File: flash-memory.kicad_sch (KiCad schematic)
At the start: 4 parts, among them U6 W25Q64JVZEIQ

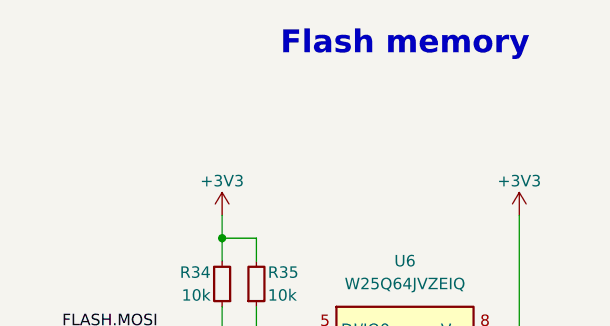
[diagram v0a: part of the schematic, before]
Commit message: [#86617] Unify captions, add TVS to USB VBUS
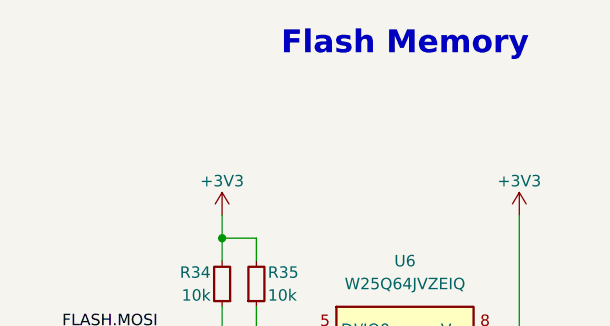
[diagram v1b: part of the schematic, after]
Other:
- note added: "Flash Memory"
- note removed: "Flash memory"
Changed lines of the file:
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@@
 		(comment 1 "www.antmicro.com")
 	)
-	(text "Flash memory"
+	(text "Flash Memory"
 		(exclude_from_sim no)
 		(at 213.36 111.76 0)

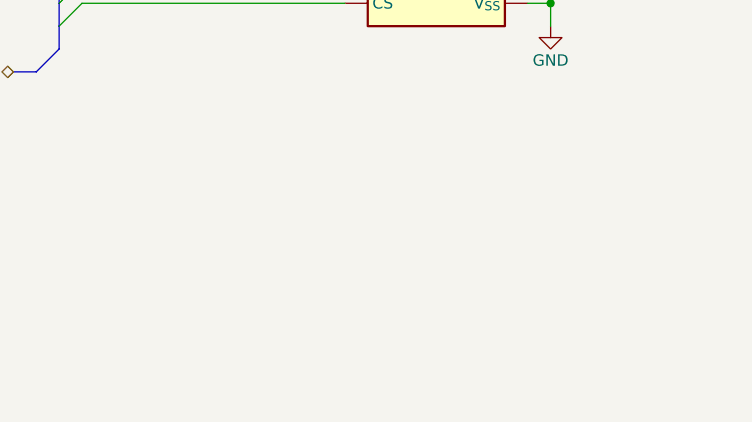
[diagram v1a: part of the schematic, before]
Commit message: [#86617] Add Tag-Connect to flash memory
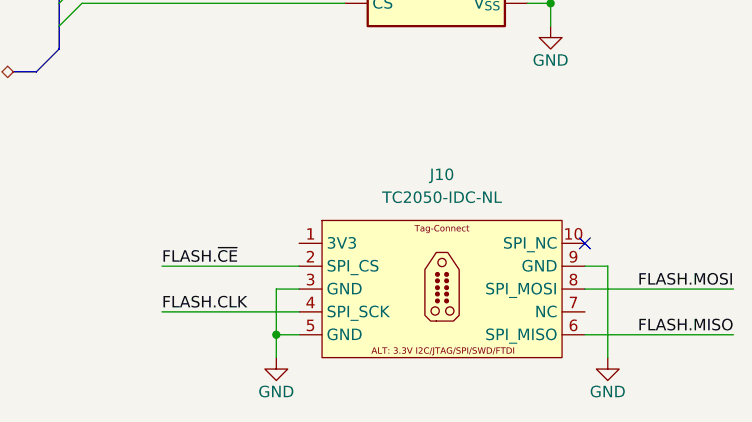
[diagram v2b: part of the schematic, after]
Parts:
- added J10: Tag-Connect_TC2050-IDC-NL_2x5_P1.27mm, antmicro-footprints:Tag-Connect_TC2050-IDC-NL_2x5_P1.27mm, symbol antmicroTestPoints:Tag-Connect_TC2050-IDC-NL_2x5_P1.27mm
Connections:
- net FLASH.CLK: now also J10.4
- net FLASH.MISO: now also J10.6
- net FLASH.MOSI: now also J10.8
- net FLASH.~{CE}: now also J10.2
- net GND: now also J10.3, J10.5, J10.9
- no-connect marks 0 -> 1

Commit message: [#86351] Rename project
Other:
- title: 10GbE Expansion -> OCuLink to 10GbE adapter
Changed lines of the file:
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@@
 	(paper "A3")
 	(title_block
-		(title "10GbE Expansion")
+		(title "OCuLink to 10GbE adapter")
 		(date "2025-11-07")
 		(rev "1.0.0")
@@
 		)
 		(instances
-			(project "10-gbe-expansion"
+			(project "OCuLink to 10GbE adapter"
 				(path "/04bda987-e5eb-48b4-9e90-d8211dc11b39/cf61e8ef-a7e0-463f-9b69-1bf3871ad792"
 					(reference "#PWR063")
@@
 		)
 		(instances
-			(project "10-gbe-expansion"
+			(project "OCuLink to 10GbE adapter"
 				(path "/04bda987-e5eb-48b4-9e90-d8211dc11b39/cf61e8ef-a7e0-463f-9b69-1bf3871ad792"
 					(reference "#PWR0338")
@@
 		)
 		(instances
-			(project "10-gbe-expansion"
+			(project "OCuLink to 10GbE adapter"
 				(path "/04bda987-e5eb-48b4-9e90-d8211dc11b39/cf61e8ef-a7e0-463f-9b69-1bf3871ad792"
 					(reference "R34")
@@
 		)
 		(instances
-			(project "10-gbe-expansion"
+			(project "OCuLink to 10GbE adapter"
 				(path "/04bda987-e5eb-48b4-9e90-d8211dc11b39/cf61e8ef-a7e0-463f-9b69-1bf3871ad792"
 					(reference "#PWR0339")
@@
 		)
 		(instances
-			(project "10-gbe-expansion"
+			(project "OCuLink to 10GbE adapter"
 				(path "/04bda987-e5eb-48b4-9e90-d8211dc11b39/cf61e8ef-a7e0-463f-9b69-1bf3871ad792"
 					(reference "#PWR064")
@@
 		)
 		(instances
-			(project "10-gbe-expansion"
+			(project "OCuLink to 10GbE adapter"
 				(path "/04bda987-e5eb-48b4-9e90-d8211dc11b39/cf61e8ef-a7e0-463f-9b69-1bf3871ad792"
 					(reference "C47")
@@
 		)
 		(instances
-			(project "10-gbe-expansion"
+			(project "OCuLink to 10GbE adapter"
 				(path "/04bda987-e5eb-48b4-9e90-d8211dc11b39/cf61e8ef-a7e0-463f-9b69-1bf3871ad792"
 					(reference "J10")
@@
 		)
 		(instances
-			(project "10-gbe-expansion"
+			(project "OCuLink to 10GbE adapter"
 				(path "/04bda987-e5eb-48b4-9e90-d8211dc11b39/cf61e8ef-a7e0-463f-9b69-1bf3871ad792"
 					(reference "#PWR065")

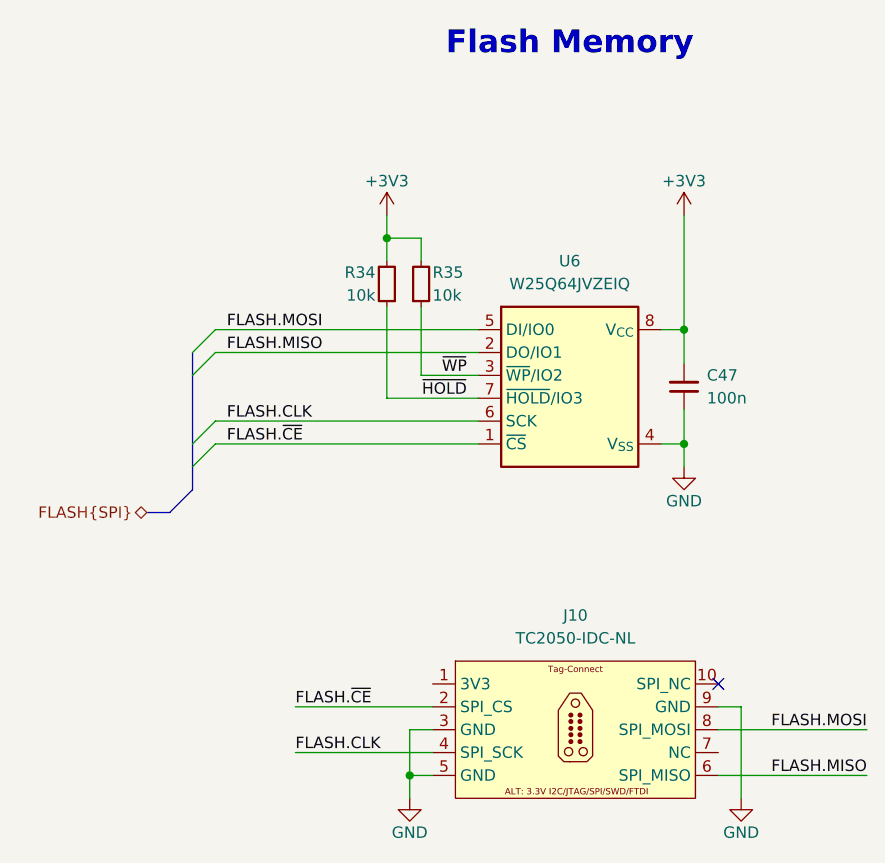
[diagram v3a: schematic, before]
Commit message: [#86617] Change flash memory to AT25DF641A-SH
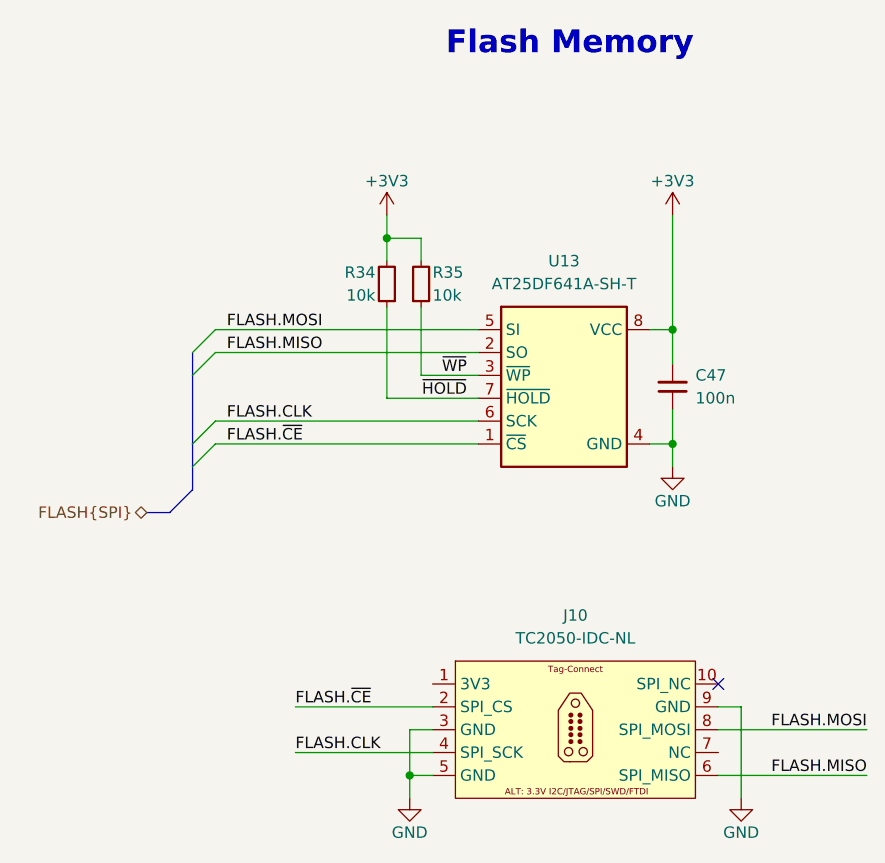
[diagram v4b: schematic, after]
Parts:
- removed U6: W25Q64JVZEIQ, antmicro-footprints:WSON-8_6x8x0.5mm_P1.27mm, symbol antmicroMemory:W25Q64JVZEIQ
- added U13: AT25DF641A-SH, antmicro-footprints:SOIC-8_5.3x5.3x2mm_P1.27mm, symbol antmicroMemory:AT25DF641A-SH
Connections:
- net +3V3: now also U13.8 (VCC)
- net FLASH.CLK: now also U13.6 (SCK)
- net FLASH.MISO: now also U13.2 (SO)
- net FLASH.MOSI: now also U13.5 (SI)
- net FLASH.~{CE}: now also U13.1 (~{CS})
- net GND: now also U13.4 (GND)
- net ~{HOLD}: now also U13.7 (~{HOLD})
- net ~{WP}: now also U13.3 (~{WP})
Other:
- moved on the sheet: C47

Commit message: [#86351] Connect Tag Connect 3V3 pin, clear ERC
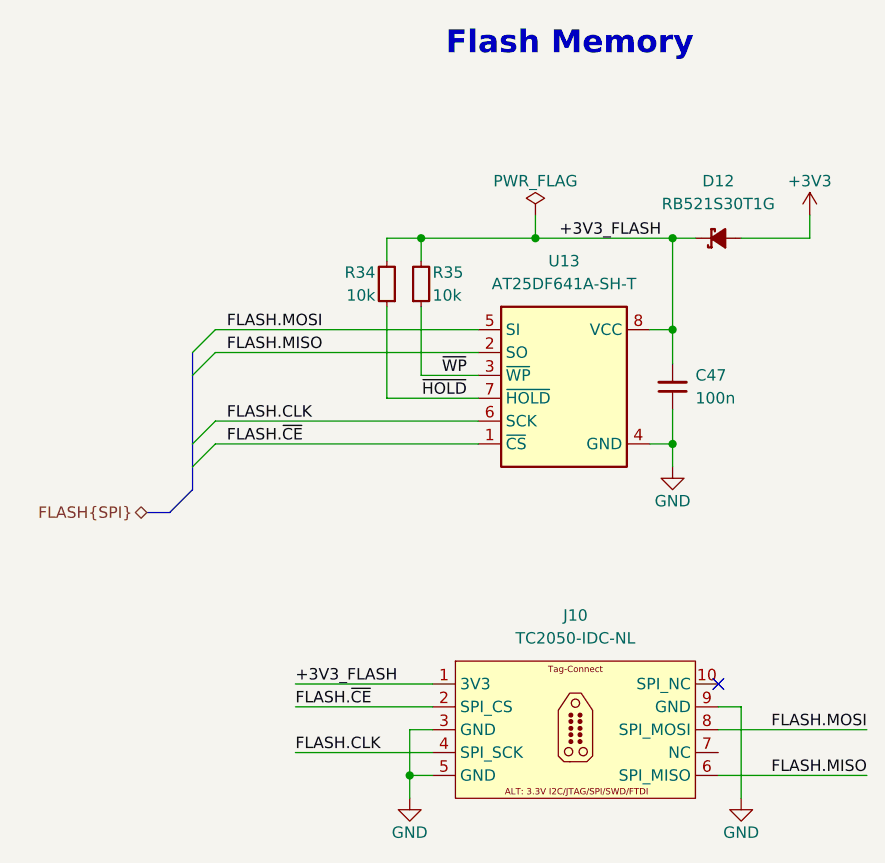
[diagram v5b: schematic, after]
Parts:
- added D12: RB521S30T1G, antmicro-footprints:SOD-523, symbol antmicroDiodesRectifiersSingle:RB521S30T1G
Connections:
- net +3V3: now also D12.2 (A); no longer C47.2, R34.2, R35.2, U13.8 (VCC)
- net +3V3_FLASH: now reaches J10.1
- net +3V3_FLASH: now also C47.2, R34.2, R35.2, U13.8 (VCC), D12.1 (C)

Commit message: [#86351] Continue layout
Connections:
- net FLASH.MISO: no longer J10.6
- net FLASH.MOSI: no longer J10.8
- net GND: no longer J10.9
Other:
- moved on the sheet: J10
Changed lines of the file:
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@@
 		(lib_id "antmicroTestPoints:Tag-Connect_TC2050-IDC-NL_2x5_P1.27mm")
 		(at 198.12 182.88 0)
+		(mirror y)
 		(unit 1)
 		(exclude_from_sim no)
@@
 		(on_board yes)
 		(dnp no)
-		(fields_autoplaced yes)
 		(property "Reference" "J10"
-			(at 213.995 175.26 0)
+			(at 182.245 175.26 0)
 			(effects
 				(font
@@
 		)
 		(property "Value" "Tag-Connect_TC2050-IDC-NL_2x5_P1.27mm"
-			(at 237.49 186.69 0)
+			(at 158.75 186.69 0)
 			(effects
 				(font
@@
 		)
 		(property "Footprint" "antmicro-footprints:Tag-Connect_TC2050-IDC-NL_2x5_P1.27mm"
-			(at 237.49 189.23 0)
+			(at 158.75 189.23 0)
 			(effects
 				(font
@@
 		)
 		(property "Datasheet" "https://www.tag-connect.com/wp-content/uploads/bsk-pdf-manager/TC2050-IDC-NL_Datasheet_8.pdf"
-			(at 237.49 191.77 0)
+			(at 158.75 191.77 0)
 			(effects
 				(font
@@
 		)
 		(property "Description" "Tag Connect 2x5 1.27mm terminal"
-			(at 237.49 204.47 0)
+			(at 158.75 204.47 0)
 			(effects
 				(font
@@
 		)
 		(property "MPN" "TC2050-IDC-NL"
-			(at 213.995 177.8 0)
+			(at 182.245 177.8 0)
 			(effects
 				(font
@@
 		)
 		(property "Manufacturer" "Tag Connect"
-			(at 237.49 196.85 0)
+			(at 158.75 196.85 0)
 			(effects
 				(font
@@
 		)
 		(property "Author" "Antmicro"
-			(at 237.49 199.39 0)
+			(at 158.75 199.39 0)
 			(effects
 				(font
@@
 		)
 		(property "License" "Apache-2.0"
-			(at 237.49 201.93 0)
+			(at 158.75 201.93 0)
 			(effects
 				(font

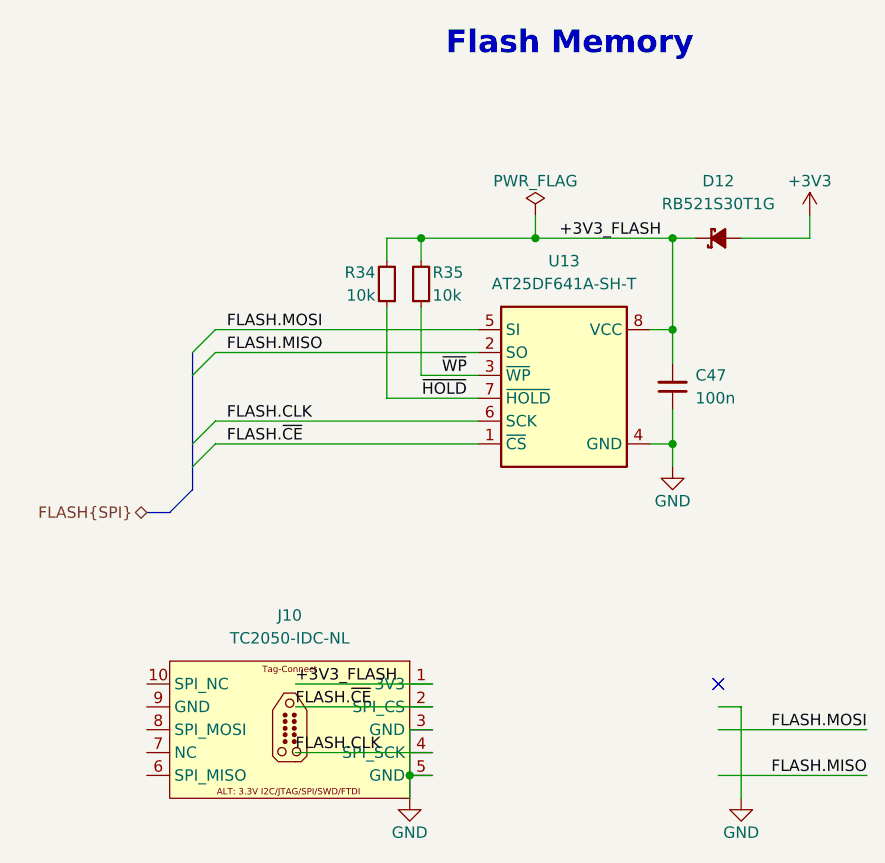
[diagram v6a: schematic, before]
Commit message: [#86351] Minor BOM consolidation
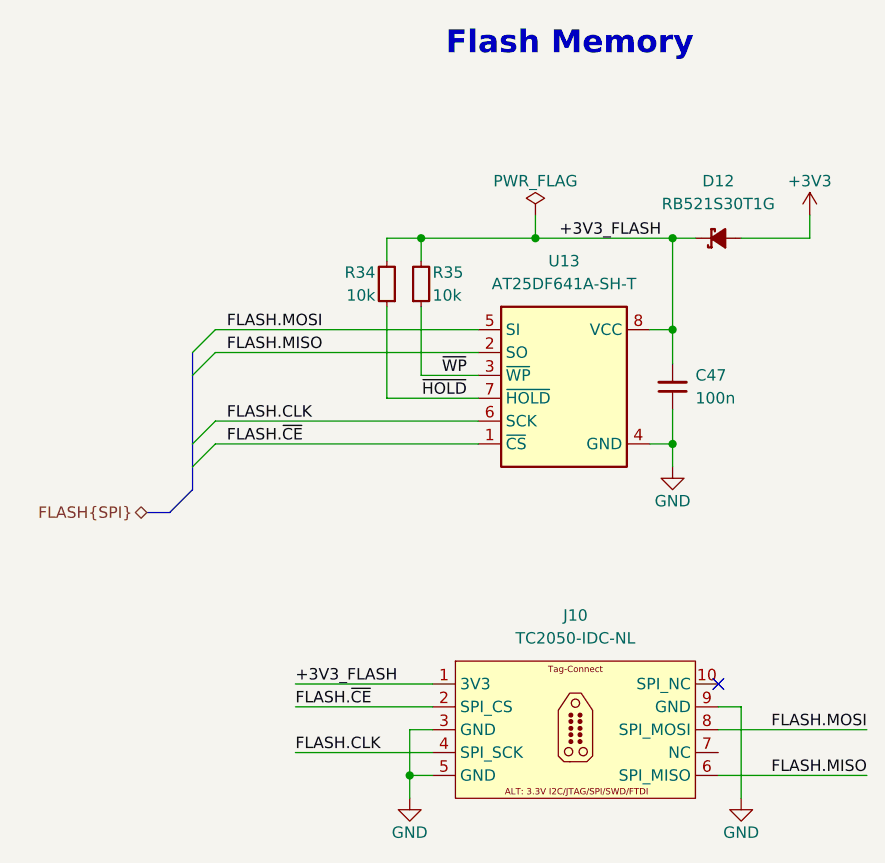
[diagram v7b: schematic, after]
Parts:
- C47: value C_100n_16V_X7R_0402 -> C_100n_0402; symbol antmicroCapacitors0402:C_100n_16V_X7R_0402 -> antmicroCapacitors0402:C_100n_0402; Dielectric X7R -> X5R; MPN C0402C104J4RAC7411 -> GRM155R61H104KE14D; Manufacturer KEMET -> Murata; Voltage 16V -> 50V
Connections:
- net FLASH.MISO: now also J10.6
- net FLASH.MOSI: now also J10.8
- net GND: now also J10.9
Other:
- moved on the sheet: J10
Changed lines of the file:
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@@
 	)
 	(symbol
-		(lib_id "antmicroCapacitors0402:C_100n_16V_X7R_0402")
+		(lib_id "antmicroCapacitors0402:C_100n_0402")
 		(at 224.79 152.4 90)
 		(unit 1)
@@
 			)
 		)
-		(property "Value" "C_100n_16V_X7R_0402"
+		(property "Value" "C_100n_0402"
 			(at 247.65 137.16 0)
 			(effects
@@
 			)
 		)
-		(property "Datasheet" "https://www.kemet.com/en/us/capacitors/product/C0402C104J4RAC7411.html"
+		(property "Datasheet" "https://www.murata.com/products/productdetail?partno=GRM155R61H104KE14%23"
 			(at 252.73 137.16 0)
 			(effects
@@
 			)
 		)
-		(property "Description" "SMD Multilayer Ceramic Capacitor, 100nF, 50V, 0402, ±5%, X7R"
+		(property "Description" "SMD Multilayer Ceramic Capacitor, 0.1 µF, 50 V, 0402 [1005 Metric], ± 10%, X5R, GRM Series"
 			(at 224.79 152.4 0)
 			(effects
@@
 			)
 		)
-		(property "MPN" "C0402C104J4RAC7411"
+		(property "MPN" "GRM155R61H104KE14D"
 			(at 255.27 137.16 0)
 			(effects
@@
 			)
 		)
-		(property "Voltage" "16V"
+		(property "Voltage" "50V"
 			(at 234.95 137.16 0)
 			(effects
@@
 			)
 		)
-		(property "Dielectric" "X7R"
+		(property "Dielectric" "X5R"
 			(at 237.49 137.16 0)
 			(effects
@@
 			)
 		)
-		(property "Manufacturer" "KEMET"
+		(property "Manufacturer" "Murata"
 			(at 240.03 137.16 0)
 			(effects
@@
 		(lib_id "antmicroTestPoints:Tag-Connect_TC2050-IDC-NL_2x5_P1.27mm")
 		(at 198.12 182.88 0)
-		(mirror y)
 		(unit 1)
 		(exclude_from_sim no)
@@
 		(dnp no)
 		(property "Reference" "J10"
-			(at 182.245 175.26 0)
+			(at 213.995 175.26 0)
 			(effects
 				(font
@@
 		)
 		(property "Value" "Tag-Connect_TC2050-IDC-NL_2x5_P1.27mm"
-			(at 158.75 186.69 0)
+			(at 237.49 186.69 0)
 			(effects
 				(font
@@
 		)
 		(property "Footprint" "antmicro-footprints:Tag-Connect_TC2050-IDC-NL_2x5_P1.27mm"
-			(at 158.75 189.23 0)
+			(at 237.49 189.23 0)
 			(effects
 				(font
@@
 		)
 		(property "Datasheet" "https://www.tag-connect.com/wp-content/uploads/bsk-pdf-manager/TC2050-IDC-NL_Datasheet_8.pdf"
-			(at 158.75 191.77 0)
+			(at 237.49 191.77 0)
 			(effects
 				(font
@@
 		)
 		(property "Description" "Tag Connect 2x5 1.27mm terminal"
-			(at 158.75 204.47 0)
+			(at 237.49 204.47 0)
 			(effects
 				(font
@@
 		)
 		(property "MPN" "TC2050-IDC-NL"
-			(at 182.245 177.8 0)
+			(at 213.995 177.8 0)
 			(effects
 				(font
@@
 		)
 		(property "Manufacturer" "Tag Connect"
-			(at 158.75 196.85 0)
+			(at 237.49 196.85 0)
 			(effects
 				(font
@@
 		)
 		(property "Author" "Antmicro"
-			(at 158.75 199.39 0)
+			(at 237.49 199.39 0)
 			(effects
 				(font
@@
 		)
 		(property "License" "Apache-2.0"
-			(at 158.75 201.93 0)
+			(at 237.49 201.93 0)
 			(effects
 				(font
@@
 		)
 		(instances
-			(project "OCuLink to 10GbE adapter"
+			(project "oculink-to-10gbe-adapter"
 				(path "/04bda987-e5eb-48b4-9e90-d8211dc11b39/cf61e8ef-a7e0-463f-9b69-1bf3871ad792"
 					(reference "J10")
